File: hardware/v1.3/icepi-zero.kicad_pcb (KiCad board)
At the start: 4 copper layers, 65 x 30 mm, 159 parts, among them IC1 IS42S16160J-6BLI, J1 Conn_02x20_Counter_Clockwise, J2 GPDI_C_1.3, J3 USB_C_Receptacle_USB2.0_14P, J4 USB_C_Receptacle_USB2.0_14P, J5 USB_C_Receptacle_USB2.0_14P, J6 Micro_SD_Card_Det2, SW1 SW_Push, SW2 SW_Push, U1 ECP5-CABGA256, U10 TPD2EUSB30A, U12 W25Q128JVS, U2 TLV62569DBV, U3 TLV62569DBV, U4 TLV62569DBV, U5 TPD2EUSB30A, U6 PCA9306DC1, U7 TPD2EUSB30A, U8 TPD2EUSB30A, U9 FT231XQ, Y1 SG-8018CG 50.000000MHz

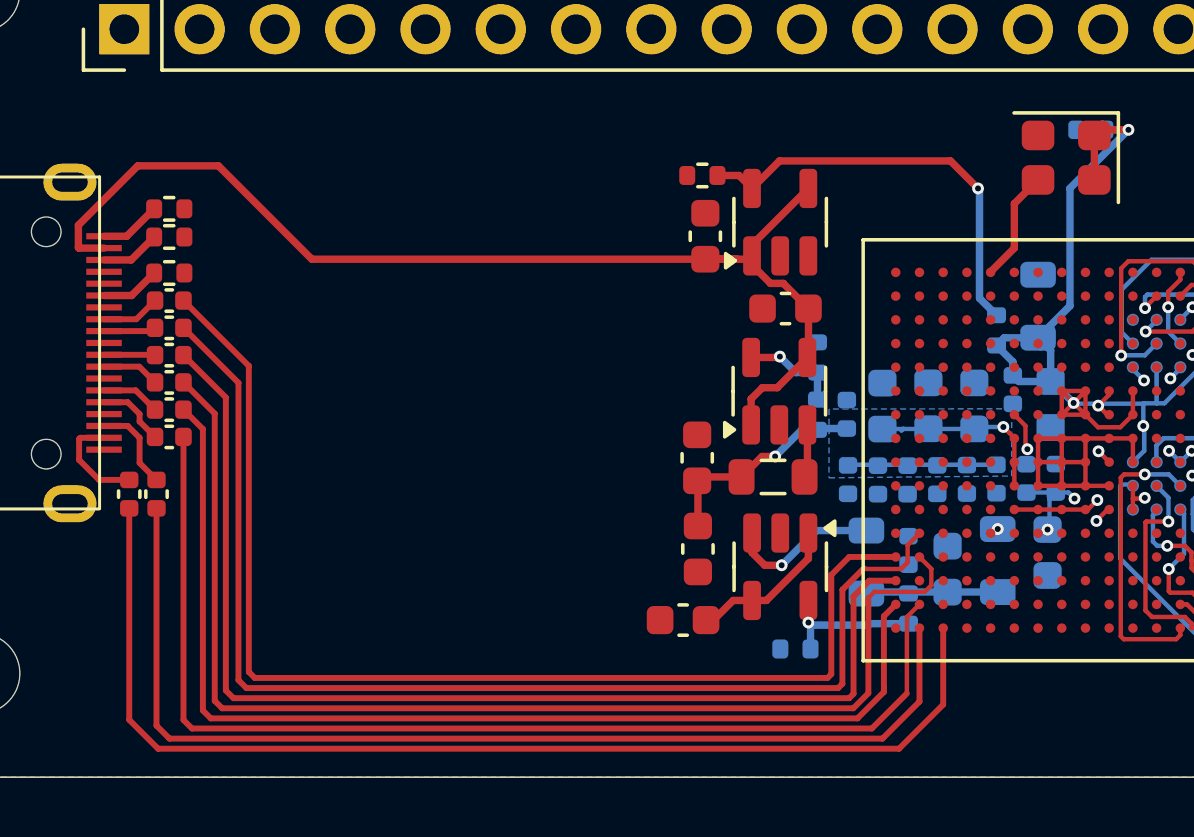
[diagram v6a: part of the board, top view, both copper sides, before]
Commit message: HDMI complete
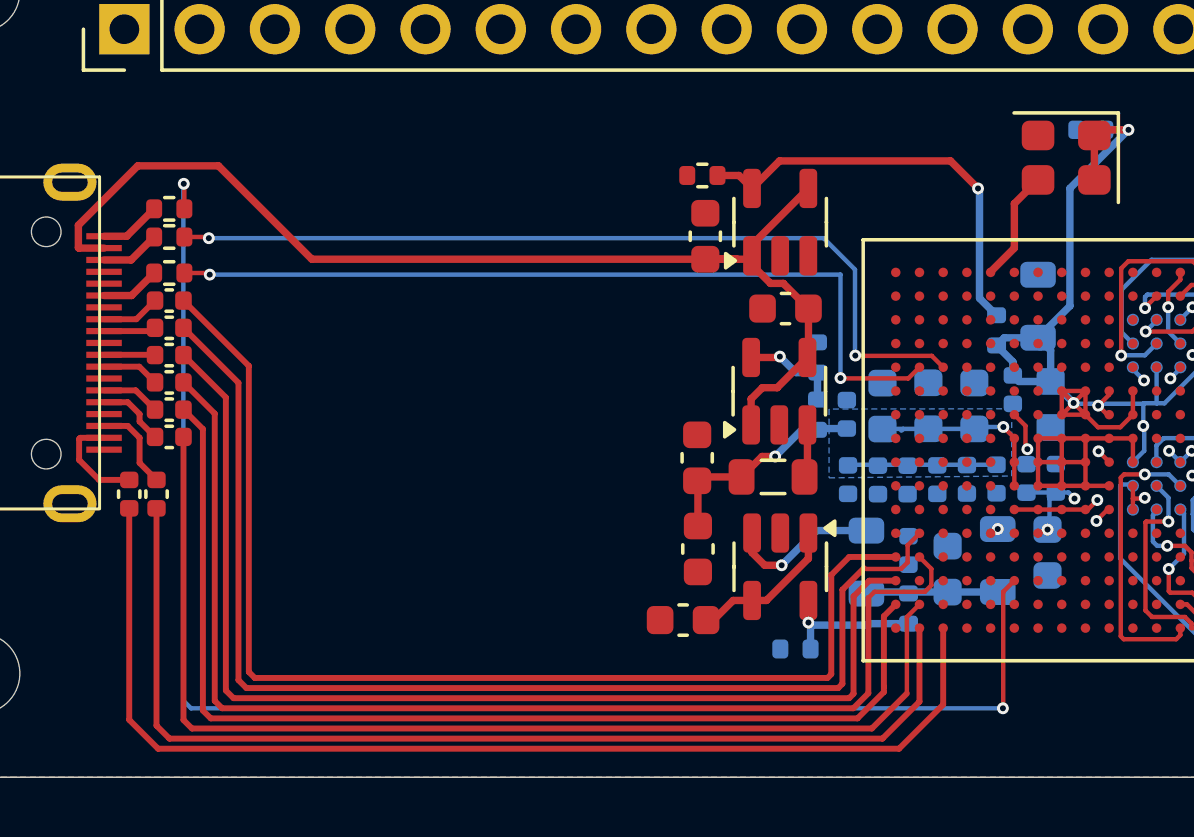
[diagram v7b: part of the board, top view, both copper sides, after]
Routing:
- net /GPDI/GPDI_HPD: track 6.53 -> 57.1 mm, vias 0 -> 2
- net /GPDI/GPDI_UTIL: track 0.00 -> 29.1 mm, vias 0 -> 2
- net /GPDI/GPDI_CEC: track 0.00 -> 28.5 mm, vias 0 -> 2
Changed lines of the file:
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@@
+	)
+	(segment
+		(start 149.518 155.682)
+		(end 126.582 155.682)
+		(width 0.2)
+		(layer "F.Cu")
+		(net 20)
+	)
+	(segment
+		(start 126.582 155.682)
+		(end 126.295 155.395)
+		(width 0.2)
+		(layer "F.Cu")
+		(net 20)
+	)
+	(segment
+		(start 150.7 151.92)
+		(end 151.125 151.495)
+		(width 0.15)
+		(layer "F.Cu")
+		(net 20)
 	)
 	(segment
@@
 	)
 	(segment
-		(start 126.582 155.682)
-		(end 126.295 155.395)
-		(width 0.2)
-		(layer "F.Cu")
-		(net 20)
-	)
-	(segment
-		(start 150.7 151.92)
-		(end 150.7 154.5)
+		(start 150.7 154.5)
+		(end 150.7 151.92)
 		(width 0.15)
 		(layer "F.Cu")
@@
 		(end 149.518 155.682)
 		(width 0.2)
-		(layer "F.Cu")
-		(net 20)
-	)
-	(segment
-		(start 149.518 155.682)
-		(end 126.582 155.682)
-		(width 0.2)
-		(layer "F.Cu")
-		(net 20)
-	)
-	(segment
-		(start 151.125 151.495)
-		(end 150.7 151.92)
-		(width 0.15)
 		(layer "F.Cu")
 		(net 20)
@@
 	)
 	(segment
+		(start 148.46 143.86)
+		(end 148.471 143.871)
+		(width 0.15)
+		(layer "F.Cu")
+		(net 103)
+	)
+	(segment
+		(start 150.749 143.871)
+		(end 151.125 143.495)
+		(width 0.15)
+		(layer "F.Cu")
+		(net 103)
+	)
+	(segment
+		(start 148.471 143.871)
+		(end 150.749 143.871)
+		(width 0.15)
+		(layer "F.Cu")
+		(net 103)
+	)
+	(segment
+		(start 126.325 140.315)
+		(end 127.125 140.315)
+		(width 0.15)
+		(layer "F.Cu")
+		(net 103)
+	)
+	(segment
+		(start 127.125 140.315)
+		(end 127.18 140.37)
+		(width 0.15)
+		(layer "F.Cu")
+		(net 103)
+	)
+	(via
+		(at 127.18 140.37)
+		(size 0.4)
+		(drill 0.2)
+		(layers "F.Cu" "B.Cu")
+		(net 103)
+	)
+	(via
+		(at 148.46 143.86)
+		(size 0.4)
+		(drill 0.2)
+		(layers "F.Cu" "B.Cu")
+		(net 103)
+	)
+	(segment
+		(start 148.46 140.37)
+		(end 127.18 140.37)
+		(width 0.15)
+		(layer "B.Cu")
+		(net 103)
+	)
+	(segment
+		(start 148.46 143.86)
+		(end 148.46 140.37)
+		(width 0.15)
+		(layer "B.Cu")
+		(net 103)
+	)
+	(segment
+		(start 127.18 140.37)
+		(end 127.12 140.37)
+		(width 0.15)
+		(layer "B.Cu")
+		(net 103)
+	)
+	(segment
+		(start 148.97 143.11)
+		(end 151.54 143.11)
+		(width 0.15)
+		(layer "F.Cu")
+		(net 104)
+	)
+	(segment
+		(start 126.325 139.1)
+		(end 127.11 139.1)
+		(width 0.15)
+		(layer "F.Cu")
+		(net 104)
+	)
+	(segment
+		(start 151.54 143.11)
+		(end 151.925 143.495)
+		(width 0.15)
+		(layer "F.Cu")
+		(net 104)
+	)
+	(segment
+		(start 127.11 139.1)
+		(end 127.15 139.14)
+		(width 0.15)
+		(layer "F.Cu")
+		(net 104)
+	)
+	(segment
+		(start 148.96 143.1)
+		(end 148.97 143.11)
+		(width 0.15)
+		(layer "F.Cu")
+		(net 104)
+	)
+	(via
+		(at 148.96 143.1)
+		(size 0.4)
+		(drill 0.2)
+		(layers "F.Cu" "B.Cu")
+		(net 104)
+	)
+	(via
+		(at 127.15 139.14)
+		(size 0.4)
+		(drill 0.2)
+		(layers "F.Cu" "B.Cu")
+		(net 104)
+	)
+	(segment
+		(start 148.95 140.2)
+		(end 148.95 143.09)
+		(width 0.15)
+		(layer "B.Cu")
+		(net 104)
+	)
+	(segment
+		(start 127.15 139.14)
+		(end 147.89 139.14)
+		(width 0.15)
+		(layer "B.Cu")
+		(net 104)
+	)
+	(segment
+		(start 148.95 143.09)
+		(end 148.96 143.1)
+		(width 0.15)
+		(layer "B.Cu")
+		(net 104)
+	)
+	(segment
+		(start 147.89 139.14)
+		(end 148.95 140.2)
+		(width 0.15)
+		(layer "B.Cu")
+		(net 104)
+	)
+	(segment
+		(start 153.95 151.07)
+		(end 153.95 154.99)
+		(width 0.15)
+		(layer "F.Cu")
+		(net 105)
+	)
+	(segment
+		(start 154.325 150.695)
+		(end 153.95 151.07)
+		(width 0.15)
+		(layer "F.Cu")
+		(net 105)
+	)
+	(segment
+		(start 126.325 138.15)
+		(end 126.325 137.325)
+		(width 0.15)
+		(layer "F.Cu")
+		(net 105)
+	)
+	(segment
+		(start 153.95 154.99)
+		(end 153.94 155)
+		(width 0.15)
+		(layer "F.Cu")
+		(net 105)
+	)
+	(segment
+		(start 126.325 137.325)
+		(end 126.305 137.305)
+		(width 0.15)
+		(layer "F.Cu")
+		(net 105)
+	)
+	(via
+		(at 153.94 155)
+		(size 0.4)
+		(drill 0.2)
+		(layers "F.Cu" "B.Cu")
+		(net 105)
+	)
+	(via
+		(at 126.305 137.305)
+		(size 0.4)
+		(drill 0.2)
+		(layers "F.Cu" "B.Cu")
+		(net 105)
+	)
+	(segment
+		(start 126.55 155)
+		(end 126.29 154.74)
+		(width 0.15)
+		(layer "B.Cu")
+		(net 105)
+	)
+	(segment
+		(start 126.29 137.32)
+		(end 126.305 137.305)
+		(width 0.15)
+		(layer "B.Cu")
+		(net 105)
+	)
+	(segment
+		(start 126.305 137.305)
+		(end 126.33 137.28)
+		(width 0.15)
+		(layer "B.Cu")
+		(net 105)
+	)
+	(segment
+		(start 126.29 154.74)
+		(end 126.29 137.32)
+		(width 0.15)
+		(layer "B.Cu")
+		(net 105)
+	)
+	(segment
+		(start 153.94 155)
+		(end 126.55 155)
+		(width 0.15)
+		(layer "B.Cu")
+		(net 105)
+	)
+	(segment

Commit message: uSD
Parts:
- C54: moved to F.Cu
- J6: moved to B.Cu
- moved J6 56.2 mm to (139.5, 154.7), turned to 180 degrees
- moved C54 54.1 mm to (140.0, 152.0), turned to 0 degrees
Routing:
- net /uSD/SD_DAT3: track 0.00 -> 25.6 mm, vias 0 -> 2
- net /uSD/SD_DET: track 0.00 -> 21.1 mm, vias 0 -> 2
- net /uSD/SD_DAT2: track 0.00 -> 20.8 mm, vias 0 -> 2
- net /uSD/SD_CMD: track 0.00 -> 16.9 mm, vias 0 -> 2
- net /uSD/SD_DAT1: track 0.00 -> 16.9 mm, vias 0 -> 2
- net /uSD/SD_CLK: track 0.00 -> 12.9 mm, vias 0 -> 2
- net /uSD/SD_DAT0: track 0.00 -> 12.0 mm, vias 0 -> 2
- net /GPDI/GPDI_HPD: track 57.1 -> 55.2 mm
- net /GPDI/GPDI_CEC: track 28.5 -> 29.7 mm
- net /GPDI/GPDI_D0+: track 40.2 -> 39.5 mm
- net +3V3: vias 9 -> 10
